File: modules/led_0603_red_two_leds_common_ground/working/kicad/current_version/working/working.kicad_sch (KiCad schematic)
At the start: 4 parts

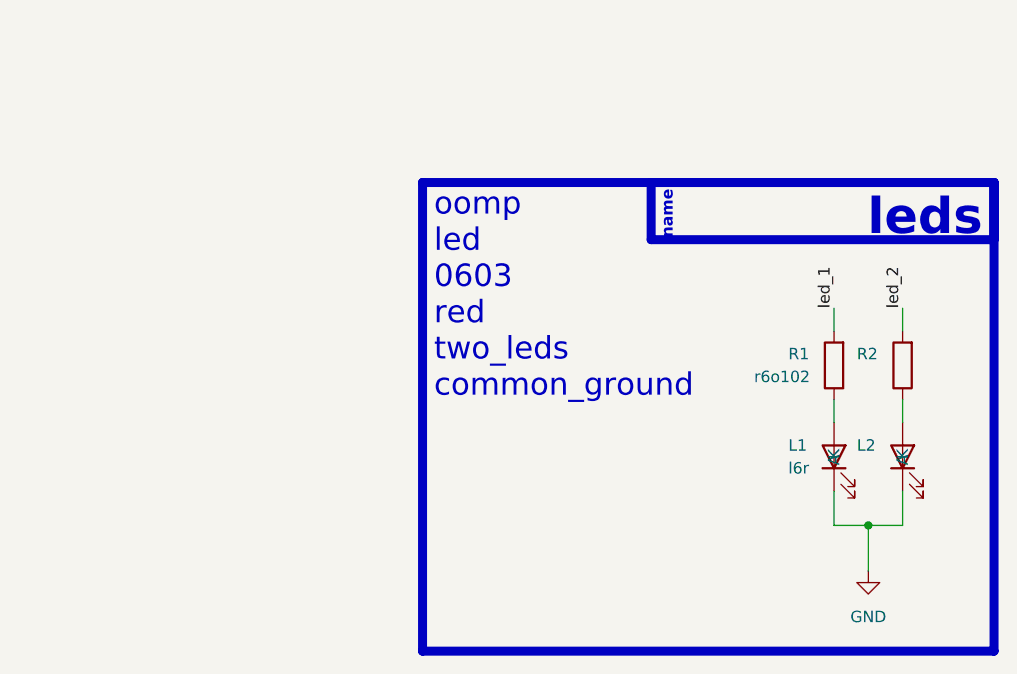
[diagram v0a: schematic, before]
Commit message: fixed formatting to be more consistent
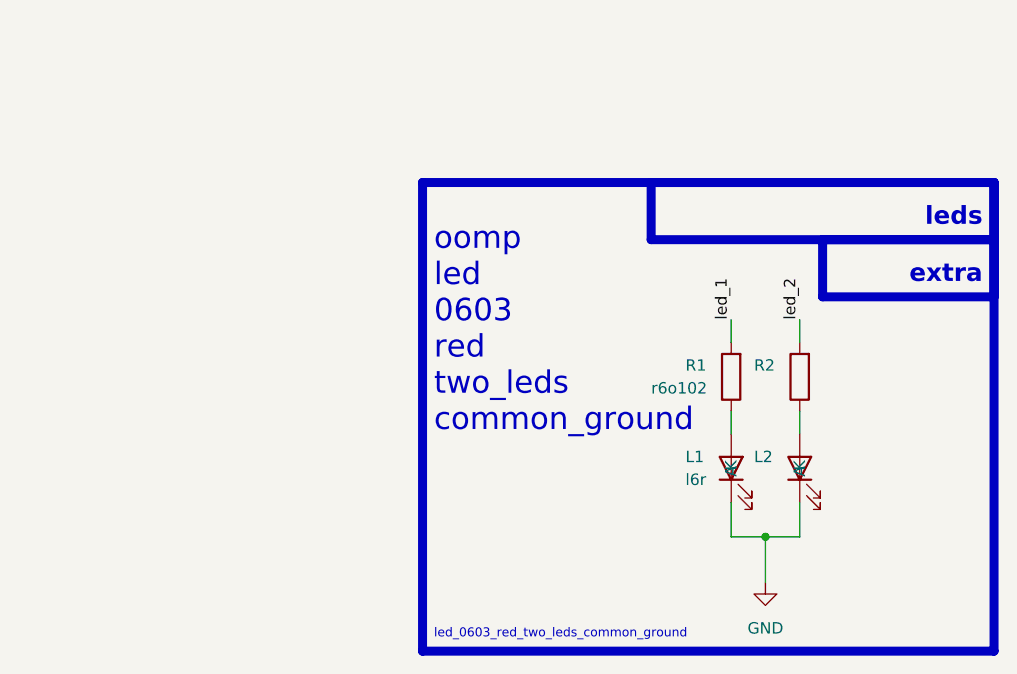
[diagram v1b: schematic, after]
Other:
- note added: "extra"
- note added: "led_0603_red_two_leds_common_ground"
- note removed: "name"
- moved on the sheet: L1, L2, R1, R2
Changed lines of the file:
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@@
 (kicad_sch (version 20230121) (generator eeschema)
   (paper "A4")
-  (junction (at 168.91 96.52) (diameter 0) (color 0 0 0 0)
+  (junction (at 157.48 97.79) (diameter 0) (color 0 0 0 0)
   )
-  (wire (pts (xy 165.1 82.55) (xy 165.1 85.09))
+  (wire (pts (xy 153.67 83.82) (xy 153.67 86.36))
     (stroke (width 0) (type default))
   )
-  (wire (pts (xy 172.72 92.71) (xy 172.72 96.52))
+  (wire (pts (xy 161.29 93.98) (xy 161.29 97.79))
     (stroke (width 0) (type default))
   )
-  (wire (pts (xy 168.91 96.52) (xy 168.91 101.6))
+  (wire (pts (xy 157.48 97.79) (xy 157.48 102.87))
     (stroke (width 0) (type default))
   )
-  (wire (pts (xy 165.1 96.52) (xy 168.91 96.52))
+  (wire (pts (xy 153.67 97.79) (xy 157.48 97.79))
     (stroke (width 0) (type default))
   )
-  (wire (pts (xy 172.72 72.39) (xy 172.72 74.93))
+  (wire (pts (xy 161.29 73.66) (xy 161.29 76.2))
     (stroke (width 0) (type default))
   )
-  (wire (pts (xy 165.1 72.39) (xy 165.1 74.93))
+  (wire (pts (xy 153.67 73.66) (xy 153.67 76.2))
     (stroke (width 0) (type default))
   )
-  (wire (pts (xy 172.72 82.55) (xy 172.72 85.09))
+  (wire (pts (xy 161.29 83.82) (xy 161.29 86.36))
     (stroke (width 0) (type default))
   )
-  (wire (pts (xy 168.91 96.52) (xy 172.72 96.52))
+  (wire (pts (xy 157.48 97.79) (xy 161.29 97.79))
     (stroke (width 0) (type default))
   )
-  (wire (pts (xy 165.1 92.71) (xy 165.1 96.52))
+  (wire (pts (xy 153.67 93.98) (xy 153.67 97.79))
     (stroke (width 0) (type default))
+  )
+  (rectangle (start 163.83 64.77) (end 182.88 71.12)
+    (stroke (width 1) (type default))
+    (fill (type none))
   )
   (rectangle (start 144.78 58.42) (end 182.88 64.77)
     (stroke (width 1) (type default))
-    (fill (type color) (color 0 0 0 0))
+    (fill (type none))
   )
   (rectangle (start 119.38 58.42) (end 182.88 110.49)
@@
     (fill (type none))
   )
-  (text "name" (at 147.32 64.77 90)
-    (effects (font (size 1.27 1.27) (thickness 0.254) bold (color 255 255 255 1)) (justify left bottom))
+  (text "extra" (at 181.61 69.85 0)
+    (effects (font (size 2 2) (thickness 0.8) bold) (justify right bottom))
   )
-  (text "oomp\nled\n0603\nred\ntwo_leds\ncommon_ground\n" (at 120.65 82.55 0)
+  (text "oomp\nled\n0603\nred\ntwo_leds\ncommon_ground\n" (at 120.65 86.36 0)
     (effects (font (size 2.5 2.5)) (justify left bottom))
   )
-  (text "leds" (at 181.61 64.77 0)
-    (effects (font (size 4 4) (thickness 0.8) bold (color 255 255 255 1)) (justify right bottom))
+  (text "led_0603_red_two_leds_common_ground" (at 120.65 109.22 0)
+    (effects (font (size 1 1)) (justify left bottom))
   )
-  (label "led_2" (at 172.72 72.39 90) (fields_autoplaced)
+  (text "leds" (at 181.61 63.5 0)
+    (effects (font (size 2 2) (thickness 0.8) bold) (justify right bottom))
+  )
+  (label "led_2" (at 161.29 73.66 90) (fields_autoplaced)
     (effects (font (size 1.27 1.27)) (justify left bottom))
   )
-  (label "led_1" (at 165.1 72.39 90) (fields_autoplaced)
+  (label "led_1" (at 153.67 73.66 90) (fields_autoplaced)
     (effects (font (size 1.27 1.27)) (justify left bottom))
   )
-  (symbol (lib_id "oomlout_oomp_part_symbols:l6r_electronic_led_0603_red") (at 172.72 88.9 90) (unit 1)
+  (symbol (lib_id "oomlout_oomp_part_symbols:l6r_electronic_led_0603_red") (at 161.29 90.17 90) (unit 1)
     (in_bom yes) (on_board yes) (dnp no)
-    (property "Reference" "L2" (at 167.64 87.63 90)
+    (property "Reference" "L2" (at 156.21 88.9 90)
       (effects (font (size 1.27 1.27)) (justify right))
     )
-    (property "Value" "l6r" (at 167.64 90.17 90)
+    (property "Value" "l6r" (at 156.21 91.44 90)
       (effects (font (size 1.27 1.27)) (justify right) hide)
     )
-    (property "Footprint" "l6r_electronic_led_0603_red" (at 172.72 88.9 0)
+    (property "Footprint" "l6r_electronic_led_0603_red" (at 161.29 90.17 0)
       (effects (font (size 1.27 1.27)) hide)
     )
-    (property "Datasheet" "https://github.com/oomlout/oomlout_oomp_v3/parts/electronic_led_0603_red/datasheet.pdf" (at 172.72 88.9 0)
+    (property "Datasheet" "https://github.com/oomlout/oomlout_oomp_v3/parts/electronic_led_0603_red/datasheet.pdf" (at 161.29 90.17 0)
       (effects (font (size 1.27 1.27)) hide)
     )
@@
     )
   )
-  (symbol (lib_id "oomlout_oomp_part_symbols:l6r_electronic_led_0603_red") (at 165.1 88.9 90) (unit 1)
+  (symbol (lib_id "oomlout_oomp_part_symbols:l6r_electronic_led_0603_red") (at 153.67 90.17 90) (unit 1)
     (in_bom yes) (on_board yes) (dnp no)
-    (property "Reference" "L1" (at 160.02 87.63 90)
+    (property "Reference" "L1" (at 148.59 88.9 90)
       (effects (font (size 1.27 1.27)) (justify right))
     )
-    (property "Value" "l6r" (at 160.02 90.17 90)
+    (property "Value" "l6r" (at 148.59 91.44 90)
       (effects (font (size 1.27 1.27)) (justify right))
     )
-    (property "Footprint" "l6r_electronic_led_0603_red" (at 165.1 88.9 0)
+    (property "Footprint" "l6r_electronic_led_0603_red" (at 153.67 90.17 0)
       (effects (font (size 1.27 1.27)) hide)
     )
-    (property "Datasheet" "https://github.com/oomlout/oomlout_oomp_v3/parts/electronic_led_0603_red/datasheet.pdf" (at 165.1 88.9 0)
+    (property "Datasheet" "https://github.com/oomlout/oomlout_oomp_v3/parts/electronic_led_0603_red/datasheet.pdf" (at 153.67 90.17 0)
       (effects (font (size 1.27 1.27)) hide)
     )
@@
     )
   )
-  (symbol (lib_id "power:GND") (at 168.91 101.6 0) (unit 1)
+  (symbol (lib_id "power:GND") (at 157.48 102.87 0) (unit 1)
     (in_bom yes) (on_board yes) (dnp no) (fields_autoplaced)
-    (property "Reference" "#PWR02" (at 168.91 107.95 0)
+    (property "Reference" "#PWR02" (at 157.48 109.22 0)
       (effects (font (size 1.27 1.27)) hide)
     )
-    (property "Value" "GND" (at 168.91 106.68 0)
+    (property "Value" "GND" (at 157.48 107.95 0)
       (effects (font (size 1.27 1.27)))
     )
-    (property "Footprint" "" (at 168.91 101.6 0)
+    (property "Footprint" "" (at 157.48 102.87 0)
       (effects (font (size 1.27 1.27)) hide)
     )
-    (property "Datasheet" "" (at 168.91 101.6 0)
+    (property "Datasheet" "" (at 157.48 102.87 0)
       (effects (font (size 1.27 1.27)) hide)
     )
@@
     )
   )
-  (symbol (lib_id "oomlout_oomp_part_symbols:r6o102_electronic_resistor_0603_1000_ohm") (at 165.1 78.74 180) (unit 1)
+  (symbol (lib_id "oomlout_oomp_part_symbols:r6o102_electronic_resistor_0603_1000_ohm") (at 153.67 80.01 180) (unit 1)
     (in_bom yes) (on_board yes) (dnp no)
-    (property "Reference" "R1" (at 160.02 77.47 0)
+    (property "Reference" "R1" (at 148.59 78.74 0)
       (effects (font (size 1.27 1.27)) (justify right))
     )
-    (property "Value" "r6o102" (at 156.21 80.01 0)
+    (property "Value" "r6o102" (at 144.78 81.28 0)
       (effects (font (size 1.27 1.27)) (justify right))
     )
-    (property "Footprint" "r6o102_electronic_resistor_0603_1000_ohm" (at 166.878 78.74 90)
+    (property "Footprint" "r6o102_electronic_resistor_0603_1000_ohm" (at 155.448 80.01 90)
       (effects (font (size 1.27 1.27)) hide)
     )
-    (property "Datasheet" "https://github.com/oomlout/oomlout_oomp_v3/parts/electronic_resistor_0603_1000_ohm/datasheet.pdf" (at 165.1 78.74 0)
+    (property "Datasheet" "https://github.com/oomlout/oomlout_oomp_v3/parts/electronic_resistor_0603_1000_ohm/datasheet.pdf" (at 153.67 80.01 0)
       (effects (font (size 1.27 1.27)) hide)
     )
@@
     )
   )
-  (symbol (lib_id "oomlout_oomp_part_symbols:r6o102_electronic_resistor_0603_1000_ohm") (at 172.72 78.74 180) (unit 1)
+  (symbol (lib_id "oomlout_oomp_part_symbols:r6o102_electronic_resistor_0603_1000_ohm") (at 161.29 80.01 180) (unit 1)
     (in_bom yes) (on_board yes) (dnp no)
-    (property "Reference" "R2" (at 167.64 77.47 0)
+    (property "Reference" "R2" (at 156.21 78.74 0)
       (effects (font (size 1.27 1.27)) (justify right))
     )
-    (property "Value" "r6o102" (at 163.83 80.01 0)
+    (property "Value" "r6o102" (at 152.4 81.28 0)
       (effects (font (size 1.27 1.27)) (justify right) hide)
     )
-    (property "Footprint" "r6o102_electronic_resistor_0603_1000_ohm" (at 174.498 78.74 90)
+    (property "Footprint" "r6o102_electronic_resistor_0603_1000_ohm" (at 163.068 80.01 90)
       (effects (font (size 1.27 1.27)) hide)
     )
-    (property "Datasheet" "https://github.com/oomlout/oomlout_oomp_v3/parts/electronic_resistor_0603_1000_ohm/datasheet.pdf" (at 172.72 78.74 0)
+    (property "Datasheet" "https://github.com/oomlout/oomlout_oomp_v3/parts/electronic_resistor_0603_1000_ohm/datasheet.pdf" (at 161.29 80.01 0)
       (effects (font (size 1.27 1.27)) hide)
     )

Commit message: schematic formatting
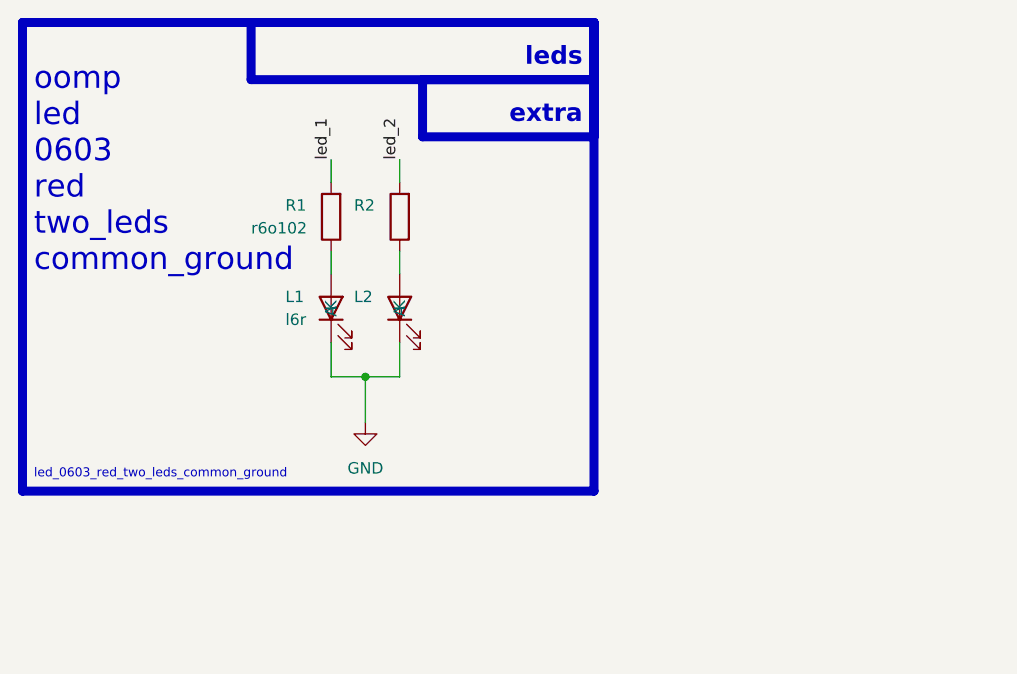
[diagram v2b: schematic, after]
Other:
- moved on the sheet: L1, L2, R1, R2
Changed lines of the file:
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@@
 (kicad_sch (version 20230121) (generator eeschema)
-  (paper "A4")
-  (junction (at 157.48 97.79) (diameter 0) (color 0 0 0 0)
+  (paper "A5")
+  (junction (at 113.03 80.01) (diameter 0) (color 0 0 0 0)
   )
-  (wire (pts (xy 153.67 83.82) (xy 153.67 86.36))
+  (wire (pts (xy 109.22 66.04) (xy 109.22 68.58))
     (stroke (width 0) (type default))
   )
-  (wire (pts (xy 161.29 93.98) (xy 161.29 97.79))
+  (wire (pts (xy 116.84 76.2) (xy 116.84 80.01))
     (stroke (width 0) (type default))
   )
-  (wire (pts (xy 157.48 97.79) (xy 157.48 102.87))
+  (wire (pts (xy 113.03 80.01) (xy 113.03 85.09))
     (stroke (width 0) (type default))
   )
-  (wire (pts (xy 153.67 97.79) (xy 157.48 97.79))
+  (wire (pts (xy 109.22 80.01) (xy 113.03 80.01))
     (stroke (width 0) (type default))
   )
-  (wire (pts (xy 161.29 73.66) (xy 161.29 76.2))
+  (wire (pts (xy 116.84 55.88) (xy 116.84 58.42))
     (stroke (width 0) (type default))
   )
-  (wire (pts (xy 153.67 73.66) (xy 153.67 76.2))
+  (wire (pts (xy 109.22 55.88) (xy 109.22 58.42))
     (stroke (width 0) (type default))
   )
-  (wire (pts (xy 161.29 83.82) (xy 161.29 86.36))
+  (wire (pts (xy 116.84 66.04) (xy 116.84 68.58))
     (stroke (width 0) (type default))
   )
-  (wire (pts (xy 157.48 97.79) (xy 161.29 97.79))
+  (wire (pts (xy 113.03 80.01) (xy 116.84 80.01))
     (stroke (width 0) (type default))
   )
-  (wire (pts (xy 153.67 93.98) (xy 153.67 97.79))
+  (wire (pts (xy 109.22 76.2) (xy 109.22 80.01))
     (stroke (width 0) (type default))
   )
-  (rectangle (start 163.83 64.77) (end 182.88 71.12)
+  (rectangle (start 119.38 46.99) (end 138.43 53.34)
     (stroke (width 1) (type default))
     (fill (type none))
   )
-  (rectangle (start 144.78 58.42) (end 182.88 64.77)
+  (rectangle (start 100.33 40.64) (end 138.43 46.99)
     (stroke (width 1) (type default))
     (fill (type none))
   )
-  (rectangle (start 119.38 58.42) (end 182.88 110.49)
+  (rectangle (start 74.93 40.64) (end 138.43 92.71)
     (stroke (width 1) (type default))
     (fill (type none))
   )
-  (rectangle (start 181.61 115.57) (end 181.61 115.57)
+  (rectangle (start 137.16 97.79) (end 137.16 97.79)
     (stroke (width 0) (type default))
     (fill (type none))
   )
-  (text "extra" (at 181.61 69.85 0)
+  (text "extra" (at 137.16 52.07 0)
     (effects (font (size 2 2) (thickness 0.8) bold) (justify right bottom))
   )
-  (text "oomp\nled\n0603\nred\ntwo_leds\ncommon_ground\n" (at 120.65 86.36 0)
+  (text "oomp\nled\n0603\nred\ntwo_leds\ncommon_ground\n" (at 76.2 68.58 0)
     (effects (font (size 2.5 2.5)) (justify left bottom))
   )
-  (text "led_0603_red_two_leds_common_ground" (at 120.65 109.22 0)
+  (text "led_0603_red_two_leds_common_ground" (at 76.2 91.44 0)
     (effects (font (size 1 1)) (justify left bottom))
   )
-  (text "leds" (at 181.61 63.5 0)
+  (text "leds" (at 137.16 45.72 0)
     (effects (font (size 2 2) (thickness 0.8) bold) (justify right bottom))
   )
-  (label "led_2" (at 161.29 73.66 90) (fields_autoplaced)
+  (label "led_2" (at 116.84 55.88 90) (fields_autoplaced)
     (effects (font (size 1.27 1.27)) (justify left bottom))
   )
-  (label "led_1" (at 153.67 73.66 90) (fields_autoplaced)
+  (label "led_1" (at 109.22 55.88 90) (fields_autoplaced)
     (effects (font (size 1.27 1.27)) (justify left bottom))
   )
-  (symbol (lib_id "oomlout_oomp_part_symbols:l6r_electronic_led_0603_red") (at 161.29 90.17 90) (unit 1)
+  (symbol (lib_id "oomlout_oomp_part_symbols:l6r_electronic_led_0603_red") (at 116.84 72.39 90) (unit 1)
     (in_bom yes) (on_board yes) (dnp no)
-    (property "Reference" "L2" (at 156.21 88.9 90)
+    (property "Reference" "L2" (at 111.76 71.12 90)
       (effects (font (size 1.27 1.27)) (justify right))
     )
-    (property "Value" "l6r" (at 156.21 91.44 90)
+    (property "Value" "l6r" (at 111.76 73.66 90)
       (effects (font (size 1.27 1.27)) (justify right) hide)
     )
-    (property "Footprint" "l6r_electronic_led_0603_red" (at 161.29 90.17 0)
+    (property "Footprint" "l6r_electronic_led_0603_red" (at 116.84 72.39 0)
       (effects (font (size 1.27 1.27)) hide)
     )
-    (property "Datasheet" "https://github.com/oomlout/oomlout_oomp_v3/parts/electronic_led_0603_red/datasheet.pdf" (at 161.29 90.17 0)
+    (property "Datasheet" "https://github.com/oomlout/oomlout_oomp_v3/parts/electronic_led_0603_red/datasheet.pdf" (at 116.84 72.39 0)
       (effects (font (size 1.27 1.27)) hide)
     )
@@
     )
   )
-  (symbol (lib_id "oomlout_oomp_part_symbols:l6r_electronic_led_0603_red") (at 153.67 90.17 90) (unit 1)
+  (symbol (lib_id "oomlout_oomp_part_symbols:l6r_electronic_led_0603_red") (at 109.22 72.39 90) (unit 1)
     (in_bom yes) (on_board yes) (dnp no)
-    (property "Reference" "L1" (at 148.59 88.9 90)
+    (property "Reference" "L1" (at 104.14 71.12 90)
       (effects (font (size 1.27 1.27)) (justify right))
     )
-    (property "Value" "l6r" (at 148.59 91.44 90)
+    (property "Value" "l6r" (at 104.14 73.66 90)
       (effects (font (size 1.27 1.27)) (justify right))
     )
-    (property "Footprint" "l6r_electronic_led_0603_red" (at 153.67 90.17 0)
+    (property "Footprint" "l6r_electronic_led_0603_red" (at 109.22 72.39 0)
       (effects (font (size 1.27 1.27)) hide)
     )
-    (property "Datasheet" "https://github.com/oomlout/oomlout_oomp_v3/parts/electronic_led_0603_red/datasheet.pdf" (at 153.67 90.17 0)
+    (property "Datasheet" "https://github.com/oomlout/oomlout_oomp_v3/parts/electronic_led_0603_red/datasheet.pdf" (at 109.22 72.39 0)
       (effects (font (size 1.27 1.27)) hide)
     )
@@
     )
   )
-  (symbol (lib_id "power:GND") (at 157.48 102.87 0) (unit 1)
+  (symbol (lib_id "power:GND") (at 113.03 85.09 0) (unit 1)
     (in_bom yes) (on_board yes) (dnp no) (fields_autoplaced)
-    (property "Reference" "#PWR02" (at 157.48 109.22 0)
+    (property "Reference" "#PWR02" (at 113.03 91.44 0)
       (effects (font (size 1.27 1.27)) hide)
     )
-    (property "Value" "GND" (at 157.48 107.95 0)
+    (property "Value" "GND" (at 113.03 90.17 0)
       (effects (font (size 1.27 1.27)))
     )
-    (property "Footprint" "" (at 157.48 102.87 0)
+    (property "Footprint" "" (at 113.03 85.09 0)
       (effects (font (size 1.27 1.27)) hide)
     )
-    (property "Datasheet" "" (at 157.48 102.87 0)
+    (property "Datasheet" "" (at 113.03 85.09 0)
       (effects (font (size 1.27 1.27)) hide)
     )
@@
     )
   )
-  (symbol (lib_id "oomlout_oomp_part_symbols:r6o102_electronic_resistor_0603_1000_ohm") (at 153.67 80.01 180) (unit 1)
+  (symbol (lib_id "oomlout_oomp_part_symbols:r6o102_electronic_resistor_0603_1000_ohm") (at 109.22 62.23 180) (unit 1)
     (in_bom yes) (on_board yes) (dnp no)
-    (property "Reference" "R1" (at 148.59 78.74 0)
+    (property "Reference" "R1" (at 104.14 60.96 0)
       (effects (font (size 1.27 1.27)) (justify right))
     )
-    (property "Value" "r6o102" (at 144.78 81.28 0)
+    (property "Value" "r6o102" (at 100.33 63.5 0)
       (effects (font (size 1.27 1.27)) (justify right))
     )
-    (property "Footprint" "r6o102_electronic_resistor_0603_1000_ohm" (at 155.448 80.01 90)
+    (property "Footprint" "r6o102_electronic_resistor_0603_1000_ohm" (at 110.998 62.23 90)
       (effects (font (size 1.27 1.27)) hide)
     )
-    (property "Datasheet" "https://github.com/oomlout/oomlout_oomp_v3/parts/electronic_resistor_0603_1000_ohm/datasheet.pdf" (at 153.67 80.01 0)
+    (property "Datasheet" "https://github.com/oomlout/oomlout_oomp_v3/parts/electronic_resistor_0603_1000_ohm/datasheet.pdf" (at 109.22 62.23 0)
       (effects (font (size 1.27 1.27)) hide)
     )
@@
     )
   )
-  (symbol (lib_id "oomlout_oomp_part_symbols:r6o102_electronic_resistor_0603_1000_ohm") (at 161.29 80.01 180) (unit 1)
+  (symbol (lib_id "oomlout_oomp_part_symbols:r6o102_electronic_resistor_0603_1000_ohm") (at 116.84 62.23 180) (unit 1)
     (in_bom yes) (on_board yes) (dnp no)
-    (property "Reference" "R2" (at 156.21 78.74 0)
+    (property "Reference" "R2" (at 111.76 60.96 0)
       (effects (font (size 1.27 1.27)) (justify right))
     )
-    (property "Value" "r6o102" (at 152.4 81.28 0)
+    (property "Value" "r6o102" (at 107.95 63.5 0)
       (effects (font (size 1.27 1.27)) (justify right) hide)
     )
-    (property "Footprint" "r6o102_electronic_resistor_0603_1000_ohm" (at 163.068 80.01 90)
+    (property "Footprint" "r6o102_electronic_resistor_0603_1000_ohm" (at 118.618 62.23 90)
       (effects (font (size 1.27 1.27)) hide)
     )
-    (property "Datasheet" "https://github.com/oomlout/oomlout_oomp_v3/parts/electronic_resistor_0603_1000_ohm/datasheet.pdf" (at 161.29 80.01 0)
+    (property "Datasheet" "https://github.com/oomlout/oomlout_oomp_v3/parts/electronic_resistor_0603_1000_ohm/datasheet.pdf" (at 116.84 62.23 0)
       (effects (font (size 1.27 1.27)) hide)
     )
